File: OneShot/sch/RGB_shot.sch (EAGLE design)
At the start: 20 parts, among them Q1 BC846ALT1SMD, Q2 BC846ALT1SMD, Q3 BC846ALT1SMD

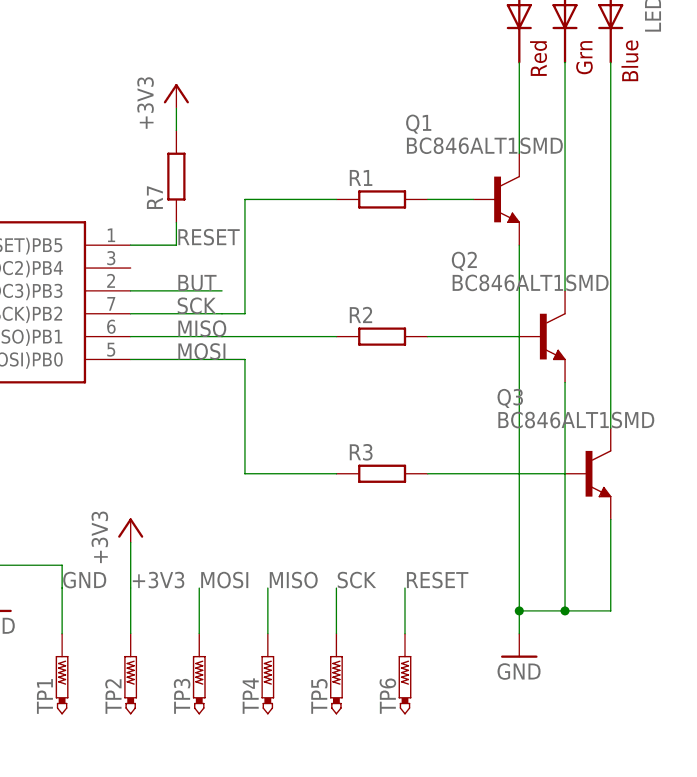
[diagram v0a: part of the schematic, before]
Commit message: Fix wire spacing
More spacing between wire for freely laser-iron production
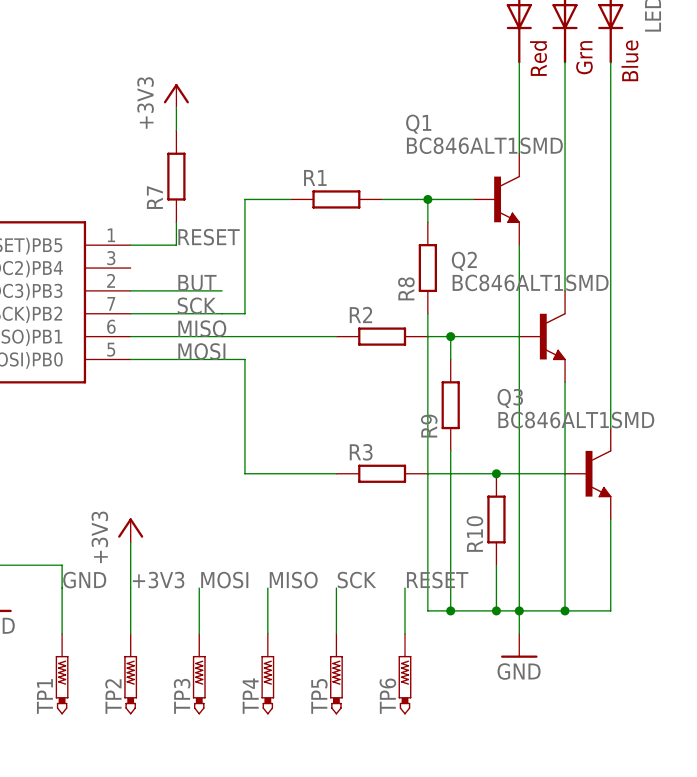
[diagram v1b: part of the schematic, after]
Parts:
- added R10, R8, R9: (no value), resistor:R-EU_M0805
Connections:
- net GND: now also R10.1, R8.1, R9.1
- net N$10: now also R9.2
- net N$11: now also R10.2
- net N$9: now also R8.2
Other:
- moved on the sheet: R1
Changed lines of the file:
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@@
 <part name="GND4" library="supply1" deviceset="GND" device=""/>
 <part name="U$2" library="SashaLib" deviceset="BAT33_1220" device=""/>
+<part name="R8" library="resistor" deviceset="R-EU_" device="M0805"/>
+<part name="R9" library="resistor" deviceset="R-EU_" device="M0805"/>
+<part name="R10" library="resistor" deviceset="R-EU_" device="M0805"/>
 </parts>
 <sheets>
@@
 <instance part="Q2" gate="G$1" x="124.46" y="58.42"/>
 <instance part="Q3" gate="G$1" x="129.54" y="43.18"/>
-<instance part="R1" gate="G$1" x="106.68" y="73.66"/>
+<instance part="R1" gate="G$1" x="101.6" y="73.66"/>
 <instance part="R2" gate="G$1" x="106.68" y="58.42"/>
 <instance part="R3" gate="G$1" x="106.68" y="43.18"/>
@@
 <instance part="GND4" gate="1" x="40.64" y="10.16"/>
 <instance part="U$2" gate="G$1" x="48.26" y="2.54"/>
+<instance part="R8" gate="G$1" x="111.76" y="66.04" rot="R90"/>
+<instance part="R9" gate="G$1" x="114.3" y="50.8" rot="R90"/>
+<instance part="R10" gate="G$1" x="119.38" y="38.1" rot="R90"/>
 </instances>
 <busses>
@@
 <junction x="121.92" y="27.94"/>
 <junction x="127" y="27.94"/>
+<pinref part="R10" gate="G$1" pin="1"/>
+<wire x1="119.38" y1="33.02" x2="119.38" y2="27.94" width="0.1524" layer="91"/>
+<wire x1="119.38" y1="27.94" x2="121.92" y2="27.94" width="0.1524" layer="91"/>
+<pinref part="R9" gate="G$1" pin="1"/>
+<wire x1="114.3" y1="45.72" x2="114.3" y2="27.94" width="0.1524" layer="91"/>
+<wire x1="114.3" y1="27.94" x2="119.38" y2="27.94" width="0.1524" layer="91"/>
+<pinref part="R8" gate="G$1" pin="1"/>
+<wire x1="111.76" y1="60.96" x2="111.76" y2="27.94" width="0.1524" layer="91"/>
+<wire x1="111.76" y1="27.94" x2="114.3" y2="27.94" width="0.1524" layer="91"/>
+<junction x="114.3" y="27.94"/>
+<junction x="119.38" y="27.94"/>
 </segment>
 <segment>
@@
 <pinref part="R1" gate="G$1" pin="2"/>
 <wire x1="116.84" y1="73.66" x2="111.76" y2="73.66" width="0.1524" layer="91"/>
+<pinref part="R8" gate="G$1" pin="2"/>
+<wire x1="111.76" y1="73.66" x2="106.68" y2="73.66" width="0.1524" layer="91"/>
+<wire x1="111.76" y1="71.12" x2="111.76" y2="73.66" width="0.1524" layer="91"/>
+<junction x="111.76" y="73.66"/>
 </segment>
 </net>
@@
 <pinref part="Q2" gate="G$1" pin="B"/>
 <pinref part="R2" gate="G$1" pin="2"/>
-<wire x1="121.92" y1="58.42" x2="111.76" y2="58.42" width="0.1524" layer="91"/>
+<wire x1="121.92" y1="58.42" x2="114.3" y2="58.42" width="0.1524" layer="91"/>
+<pinref part="R9" gate="G$1" pin="2"/>
+<wire x1="114.3" y1="58.42" x2="111.76" y2="58.42" width="0.1524" layer="91"/>
+<wire x1="114.3" y1="55.88" x2="114.3" y2="58.42" width="0.1524" layer="91"/>
+<junction x="114.3" y="58.42"/>
 </segment>
 </net>
@@
 <pinref part="Q3" gate="G$1" pin="B"/>
 <pinref part="R3" gate="G$1" pin="2"/>
-<wire x1="127" y1="43.18" x2="111.76" y2="43.18" width="0.1524" layer="91"/>
+<wire x1="127" y1="43.18" x2="119.38" y2="43.18" width="0.1524" layer="91"/>
+<pinref part="R10" gate="G$1" pin="2"/>
+<wire x1="119.38" y1="43.18" x2="111.76" y2="43.18" width="0.1524" layer="91"/>
+<junction x="119.38" y="43.18"/>
 </segment>
 </net>
@@
 <label x="83.82" y="60.96" size="1.778" layer="95"/>
 <pinref part="R1" gate="G$1" pin="1"/>
-<wire x1="101.6" y1="73.66" x2="91.44" y2="73.66" width="0.1524" layer="91"/>
+<wire x1="96.52" y1="73.66" x2="91.44" y2="73.66" width="0.1524" layer="91"/>
 <wire x1="91.44" y1="73.66" x2="91.44" y2="60.96" width="0.1524" layer="91"/>
 <wire x1="91.44" y1="60.96" x2="88.9" y2="60.96" width="0.1524" layer="91"/>
